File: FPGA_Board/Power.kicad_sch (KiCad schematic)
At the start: 0 parts

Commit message: fix 'USB 3.0' typo, add USB C connector and eFuse
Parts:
- added D1: PMEG1030EJ, Diode_SMD:D_SOD-323F, symbol Diode:PMEG1030EJ
- added J1: USB_C_Receptacle_24P, symbol Connector:USB_C_Receptacle
- added R1: 1M, FPGA_BOARD:RES_1206, symbol FPGA_Parts:RES_1206
- added R2, R3: 5.1k, symbol Device:R
- added U1: LS1205EVD33, FPGA_BOARD:DFN3x3_10L, symbol FPGA_Parts:LS1205EVD33
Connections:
- new net: D1.2 (A), J1.A4 (VBUS), J1.A9 (VBUS), J1.B4 (VBUS), J1.B9 (VBUS)
- new net: J1.A5 (CC1), R2.1
- new net: J1.B5 (CC2), R3.1
- new net: J1.SH (SHIELD), R1.2
- new net: D1.1 (K), U1.1 (IN), U1.2 (IN), U1.3 (IN)
- new net GND: J1.A1 (GND), J1.A12 (GND), J1.B1 (GND), J1.B12 (GND), R1.1, R2.2, R3.2

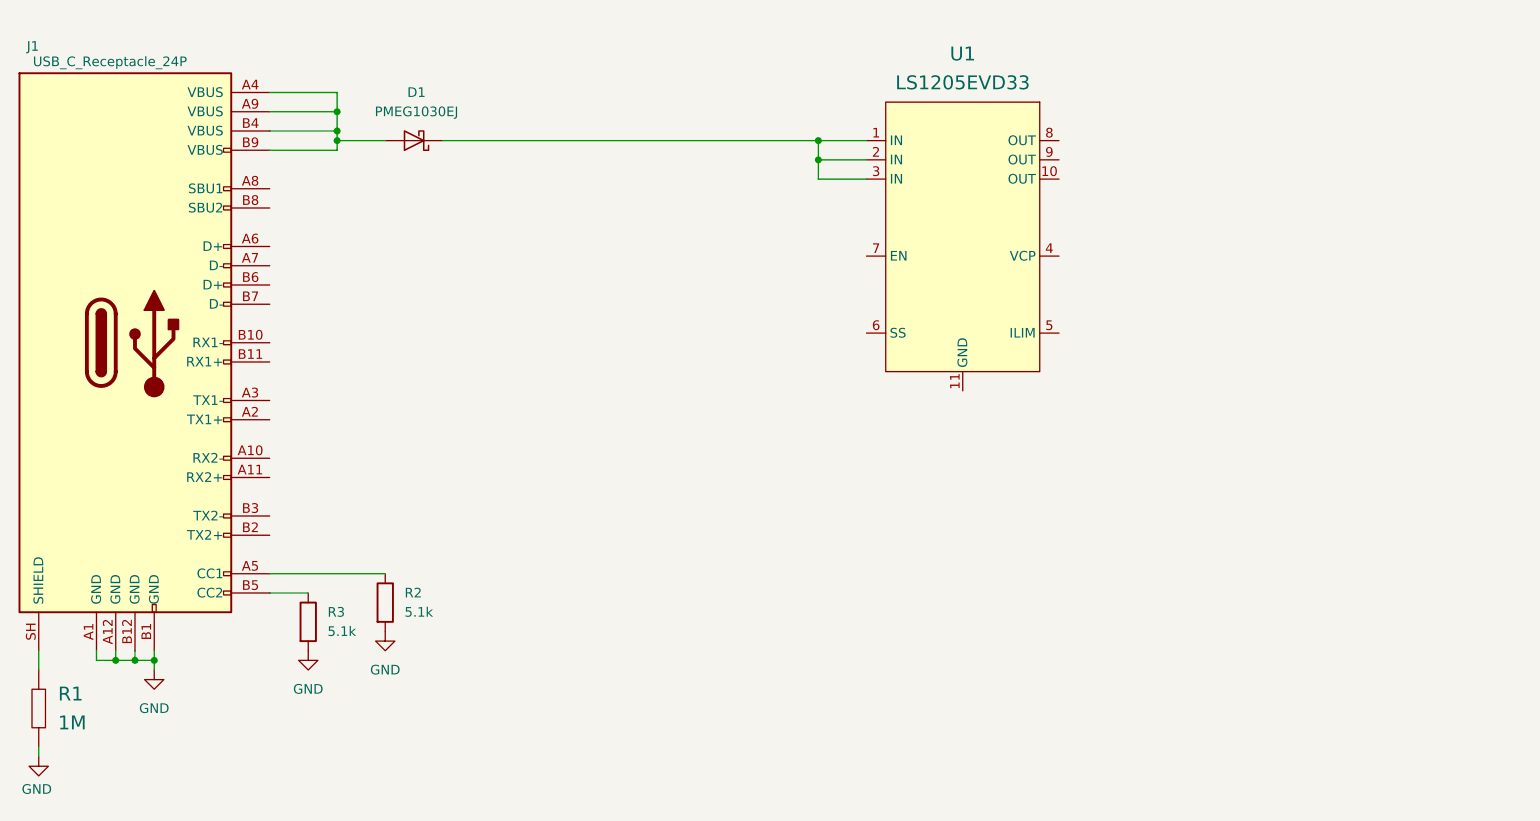
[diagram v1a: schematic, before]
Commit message: wire eFuse and USB-C, add global labels for USB D+/D-
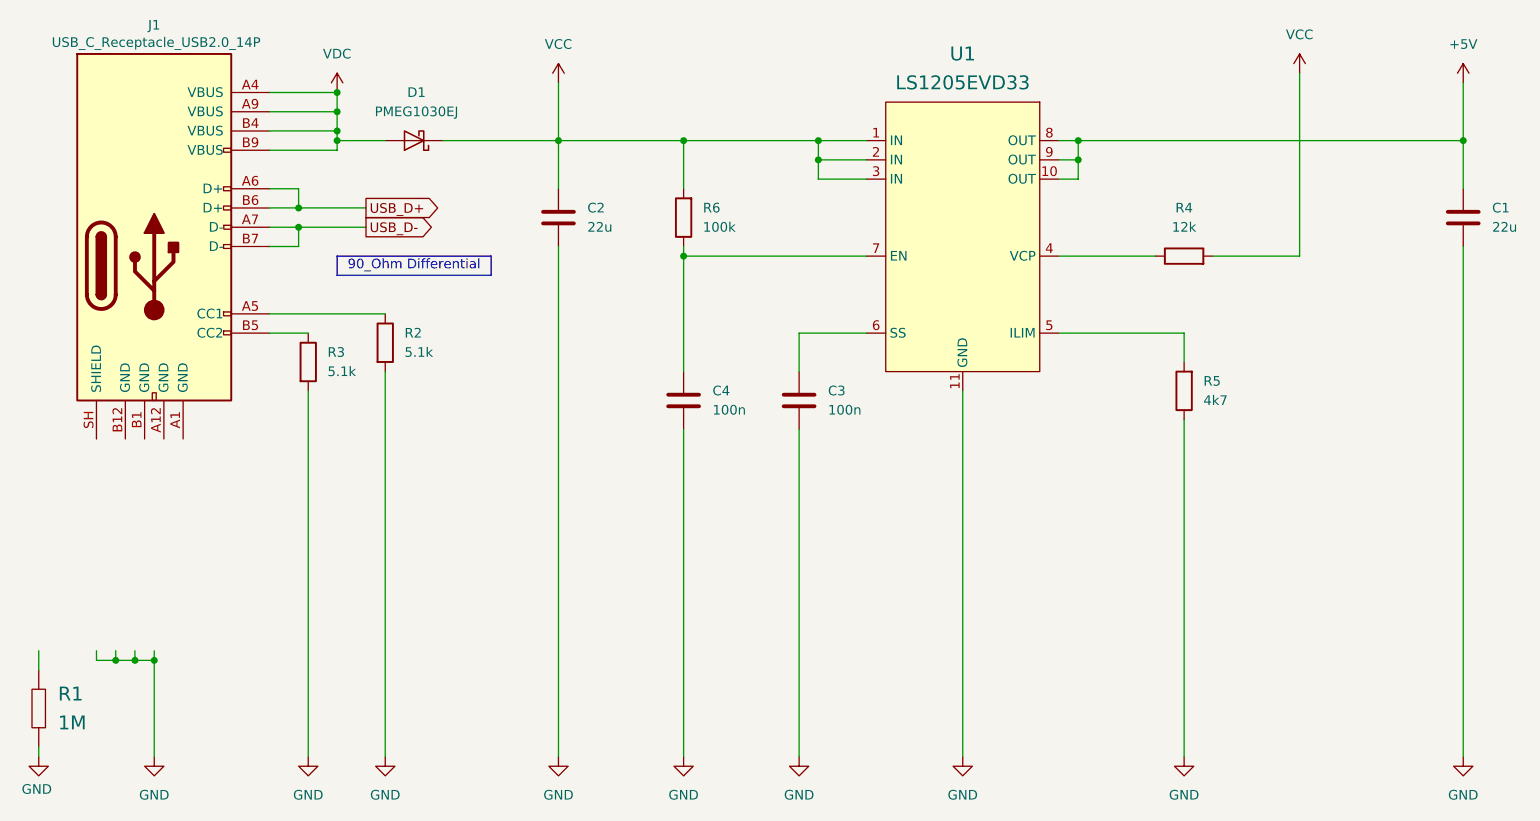
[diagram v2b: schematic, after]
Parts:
- removed J1: USB_C_Receptacle_24P, symbol Connector:USB_C_Receptacle
- added C1, C2: 22u, symbol Device:C
- added C3, C4: 100n, symbol Device:C
- added J1: USB_C_Receptacle_USB2.0_14P, symbol Connector:USB_C_Receptacle_USB2.0_14P
- added R4: 12k, symbol Device:R
- added R5: 4k7, symbol Device:R
- added R6: 100k, symbol Device:R
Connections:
- net GND: now also U1.11 (GND), C1.2, C2.2, C3.2, C4.2, R5.1
- net VDC: now reaches D1.2 (A)
- net VDC: now also J1.A4 (VBUS), J1.A9 (VBUS), J1.B4 (VBUS), J1.B9 (VBUS)
- net at R2.1: now also J1.A5 (CC1)
- net at R3.1: now also J1.B5 (CC2)
- net VCC: now reaches D1.1 (K), U1.1 (IN), U1.2 (IN), U1.3 (IN)
- net VCC: now also C2.1, R4.2, R6.2
- net +5V: now reaches U1.10 (OUT)
- net +5V: now also U1.8 (OUT), U1.9 (OUT), C1.1
- net at U1.4 (VCP): now also R4.1
- net at U1.5 (ILIM): now also R5.2
- net at U1.6 (SS): now also C3.1
- net at U1.7 (EN): now also C4.1, R6.1
- new net USB_D+: J1.A6 (D+), J1.B6 (D+)
- new net USB_D-: J1.A7 (D-), J1.B7 (D-)
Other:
- note added: "90_Ohm Differential"
- moved on the sheet: R2, R3

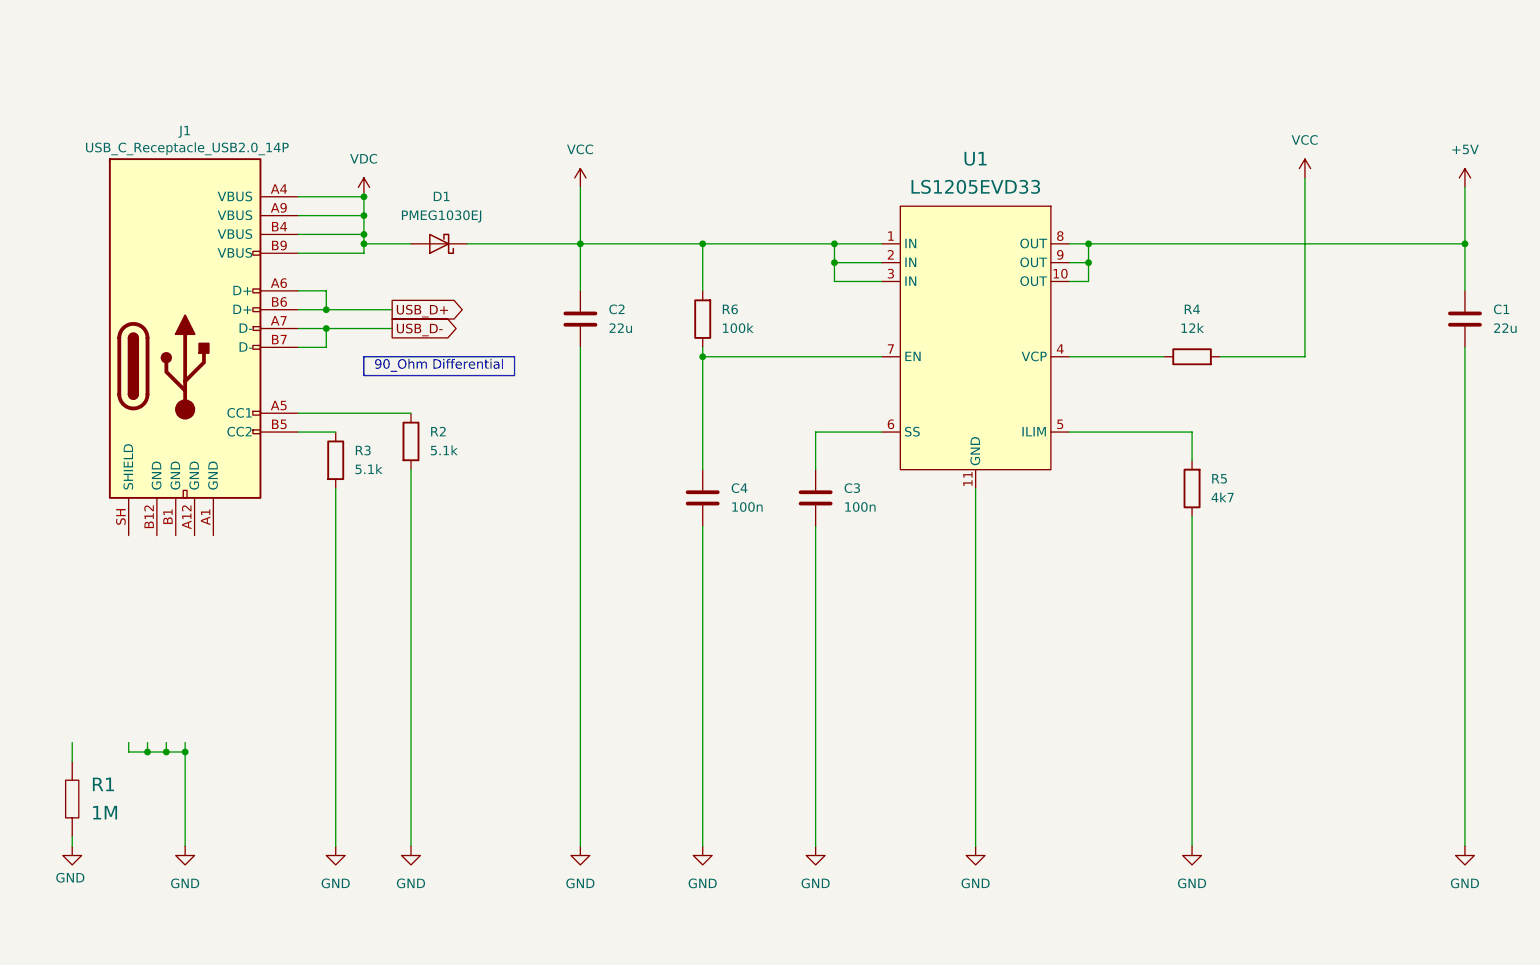
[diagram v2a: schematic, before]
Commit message: add FPGA,DDR, Decoupling capacitor symbols for power & ddr sheets. modify symbols pinout placement to clean up schematic
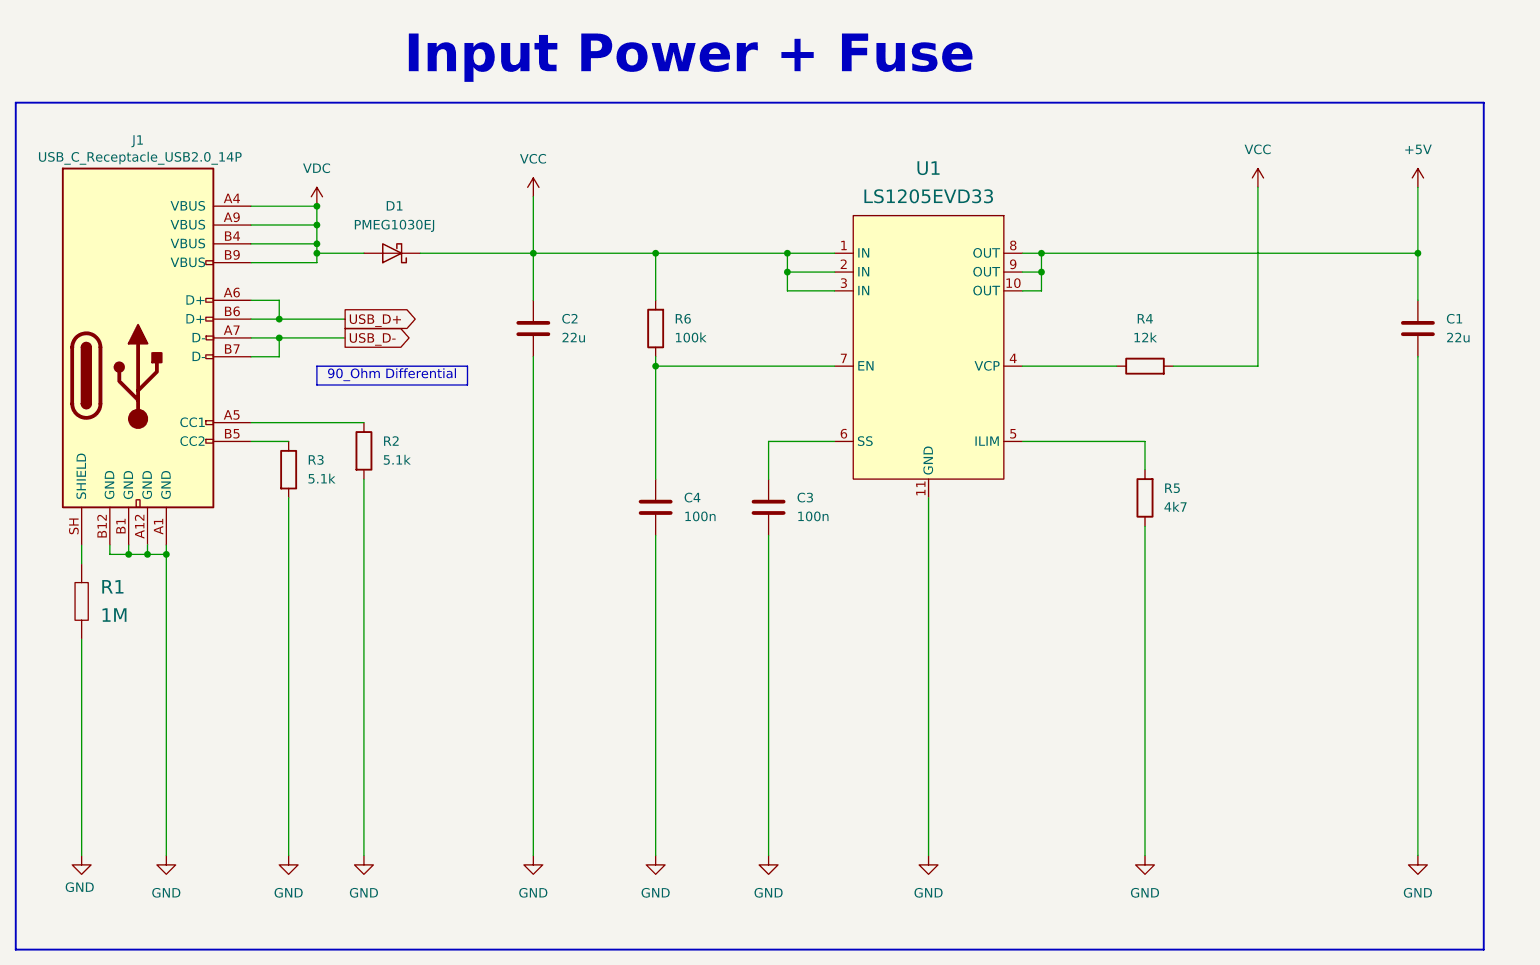
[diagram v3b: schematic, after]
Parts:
- U1: Distributor Link https://www.mouser.de/ProductDetail/Littelfuse/LS1205EVD33?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 -> https://www.mouser.com/ProductDetail/Littelfuse/LS1205EVD33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
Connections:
- net GND: now also J1.A1 (GND), J1.A12 (GND), J1.B1 (GND), J1.B12 (GND)
- net at J1.SH (SHIELD): now also R1.2
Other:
- note added: "Input Power + Fuse"
- moved on the sheet: C1, C2, C3, C4, D1, J1, R1, R2, R3, R4, R5, R6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

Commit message: Add DDR VTT power module, add Zynq power + decoupling, placed Zynq DDR
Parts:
- added C12, C14, C15, C17: 4u7, symbol Device:C
- added C13, C16: 22u, symbol Device:C
- added C18: 1n, symbol Device:C
- added R7: 100k, symbol Device:R
- added R8: 12k, symbol Device:R
- added R9: 1k, symbol Device:R
- added U6: BD3539FVM-TR, FPGA_BOARD:MSOP8, symbol FPGA_Parts:BD3539FVM-TR
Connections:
- net +5V: now also C12.1, C13.1, U6.6 (VCC), U6.7 (VTT_IN)
- net GND: now also C12.2, C13.2, C14.2, C15.2, C16.2, C17.2, C18.2, R7.1, U6.1 (GND)
- net FUSE_EN: now reaches C4.1, R6.1, U1.7 (EN)
- net USB_CC1: now reaches J1.A5 (CC1), R2.1
- net USB_CC2: now reaches J1.B5 (CC2), R3.1
- net USB_SH: now reaches J1.SH (SHIELD), R1.2
- net USB_SH: now also C18.1
- net FUSE_ILIM: now reaches R5.2, U1.5 (ILIM)
- net FUSE_SS: now reaches C3.1, U1.6 (SS)
- net FUSE_VCP: now reaches R4.1, U1.4 (VCP)
- new net +0V675: C16.1, C17.1, U6.3 (VTTS), U6.8 (VTT)
- new net +0V675_REF: C15.1, U6.4 (VREF)
- new net +1V35: R9.2
- new net DDR_VTT_EN: R7.2, R8.1, U6.2 (EN)
- new net DDR_VTT_VDDQ: C14.1, R9.1, U6.5 (VDDQ)
- new net PG_+1V35: R8.2
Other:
- note added: "DDR3L VTT"
- note added: "POWER"
- moved on the sheet: C1, C2, C3, C4, D1, J1, R1, R2, R3, R4, R5, R6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
